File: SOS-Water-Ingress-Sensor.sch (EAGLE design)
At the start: 12 parts

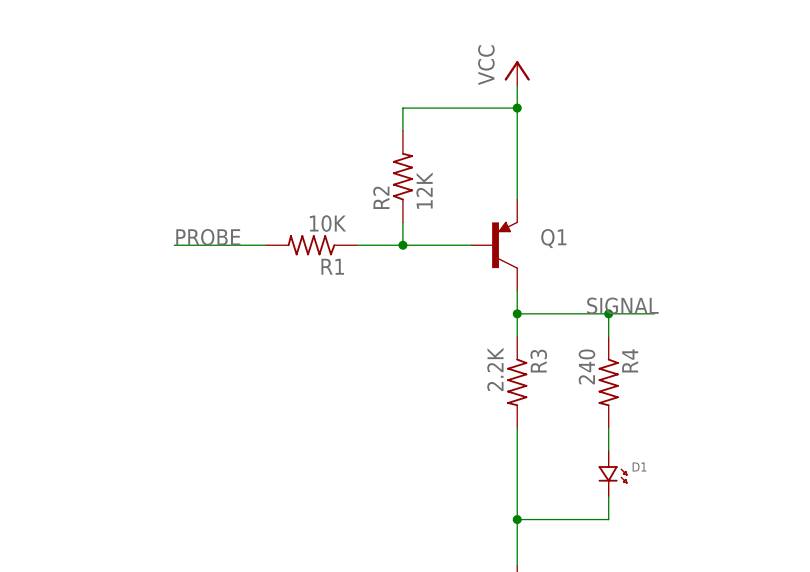
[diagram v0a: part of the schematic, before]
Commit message: Change component values and layout.
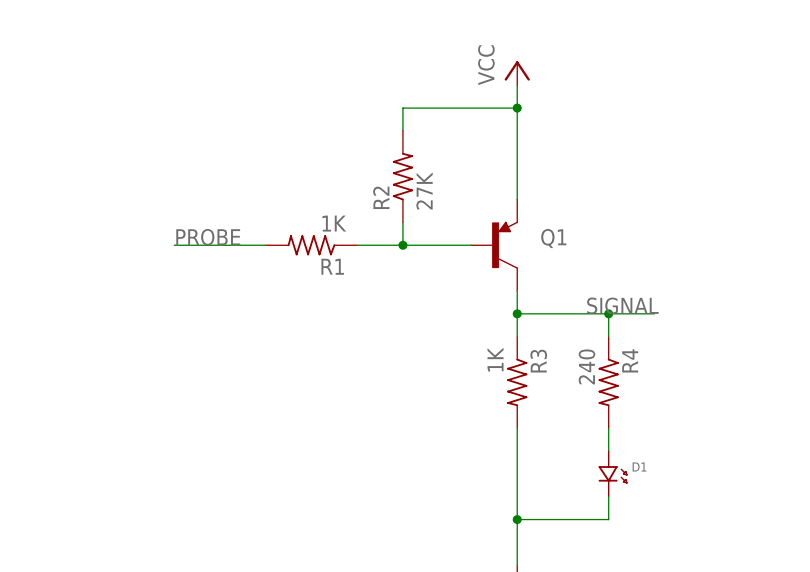
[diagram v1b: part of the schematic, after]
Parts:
- R1: value 10K -> 1K
- R2: value 12K -> 27K
- R3: value 2.2K -> 1K
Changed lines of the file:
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@@
 <?xml version="1.0" encoding="utf-8"?>
 <!DOCTYPE eagle SYSTEM "eagle.dtd">
-<eagle version="7.6.0">
+<eagle version="7.4.0">
 <drawing>
 <settings>
@@
 <part name="P+1" library="supply1" deviceset="VCC" device=""/>
 <part name="GND1" library="supply1" deviceset="GND" device=""/>
-<part name="R2" library="resistor" deviceset="R-US_" device="R0603" value="12K"/>
+<part name="R2" library="resistor" deviceset="R-US_" device="R0603" value="27K"/>
 <part name="GND2" library="supply1" deviceset="GND" device=""/>
-<part name="R1" library="resistor" deviceset="R-US_" device="R0603" value="10K"/>
+<part name="R1" library="resistor" deviceset="R-US_" device="R0603" value="1K"/>
 <part name="P+2" library="supply1" deviceset="VCC" device=""/>
 <part name="U$1" library="BlueRobotics-JST-GH" deviceset="JSH-GH-2" device="VERT"/>
 <part name="Q1" library="SparkFun-DiscreteSemi" deviceset="TRANSISTOR_PNP" device="SMD"/>
-<part name="R3" library="resistor" deviceset="R-US_" device="R0603" value="2.2K"/>
+<part name="R3" library="resistor" deviceset="R-US_" device="R0603" value="1K"/>
 <part name="U$2" library="BlueRobotics-JST-GH" deviceset="JSH-GH-2" device="VERT"/>
 <part name="U$3" library="BlueRobotics-JST-GH" deviceset="JSH-GH-2" device="VERT"/>
